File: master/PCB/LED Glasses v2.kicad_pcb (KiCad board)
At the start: 2 copper layers, 152.9 x 54.6 mm, 85 parts, among them J1 Conn_01x01_Male, J2 Conn_01x01_Male, J3 Conn_01x01_Male, J4 Conn_01x01_Male, J5 Conn_01x01_Male

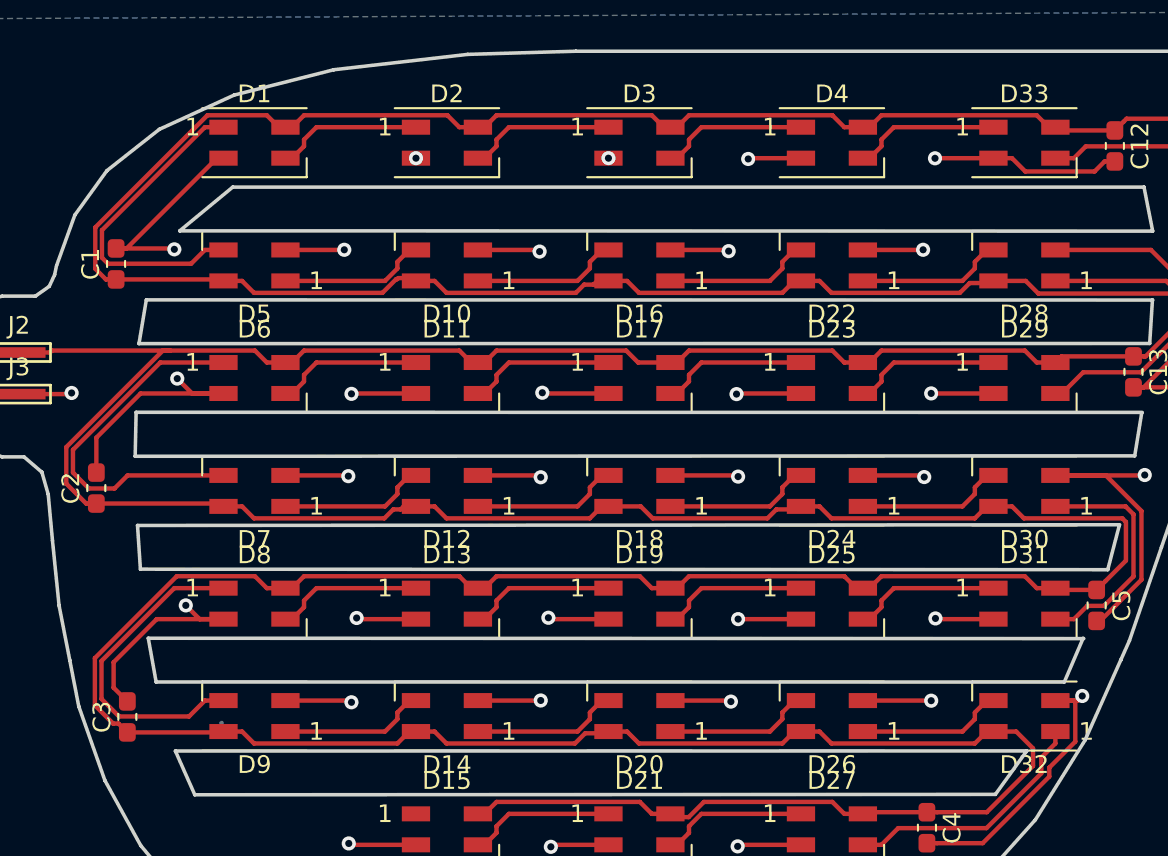
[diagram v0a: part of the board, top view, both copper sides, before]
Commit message: Added silkscreen
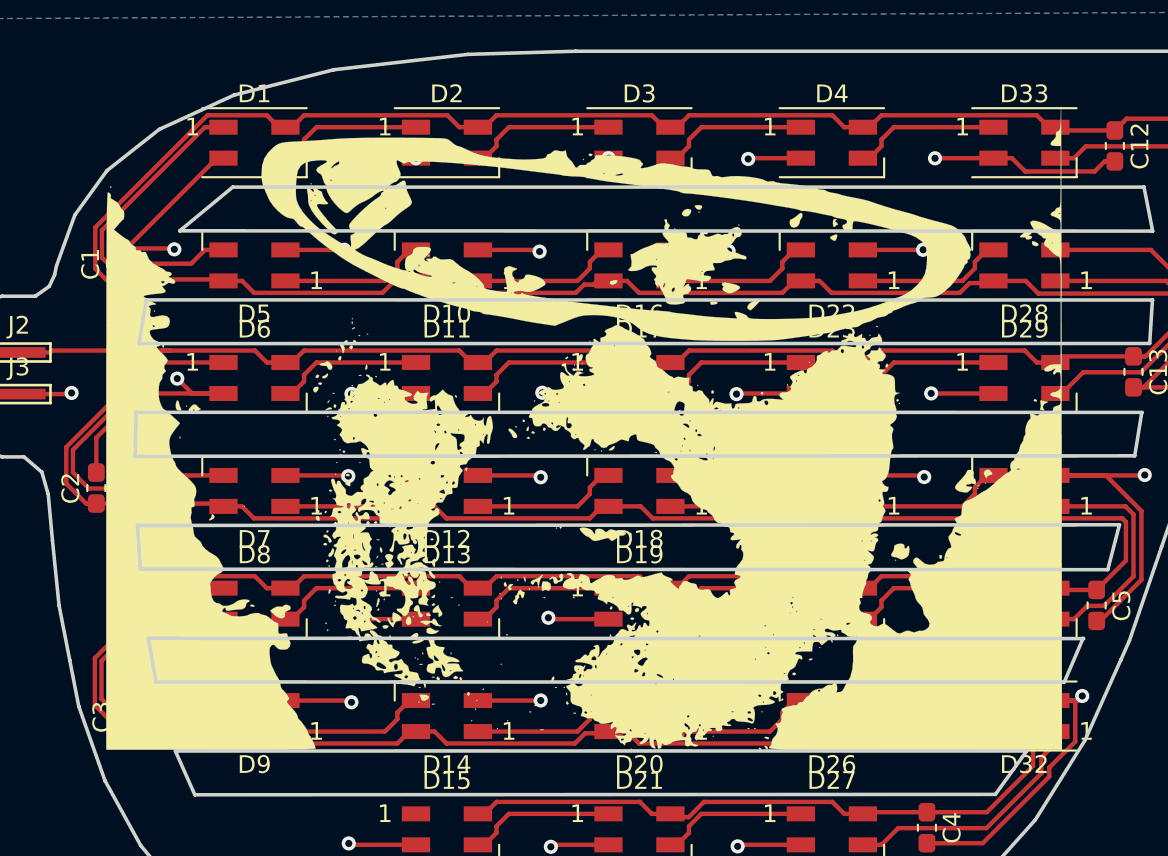
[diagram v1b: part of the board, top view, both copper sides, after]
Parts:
- added G***: LOGO-glasses, Battery:LOGO-glasses, F.Cu at (120.6, 104.3)

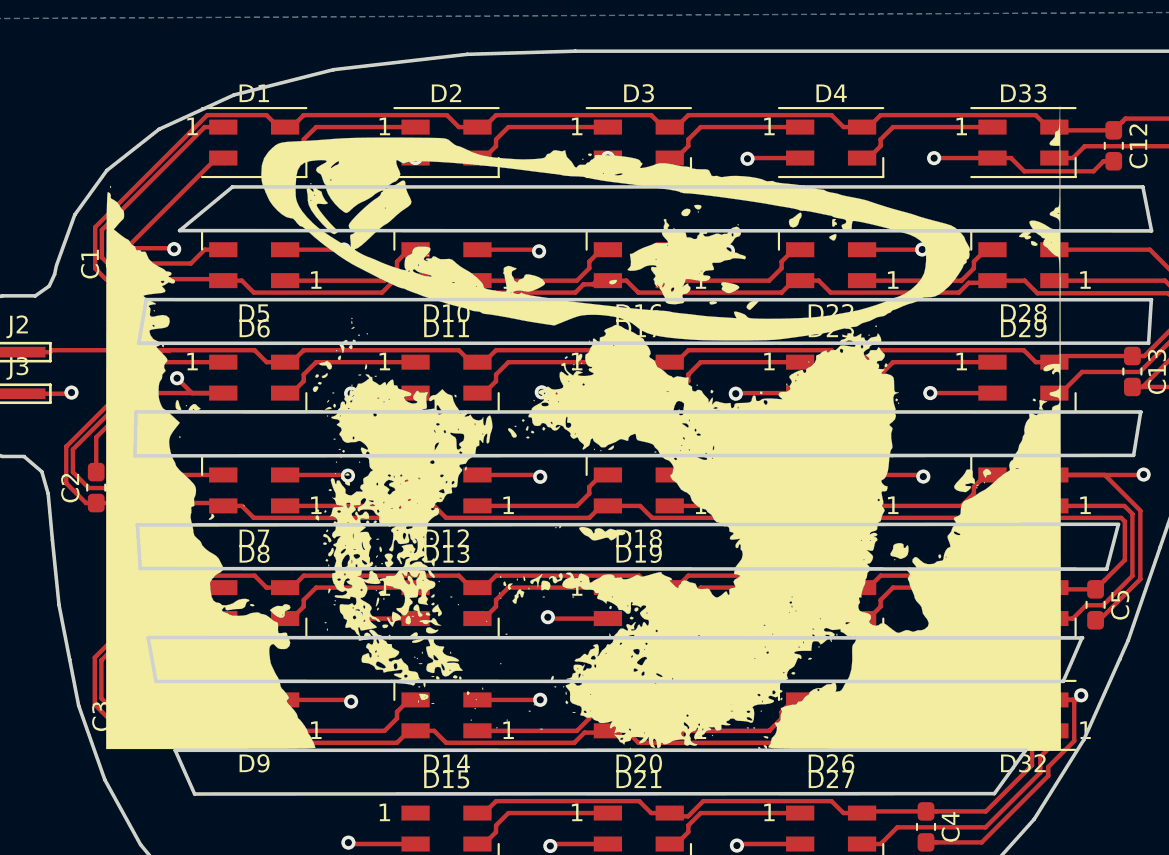
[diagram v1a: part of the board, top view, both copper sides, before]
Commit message: added silkscreen
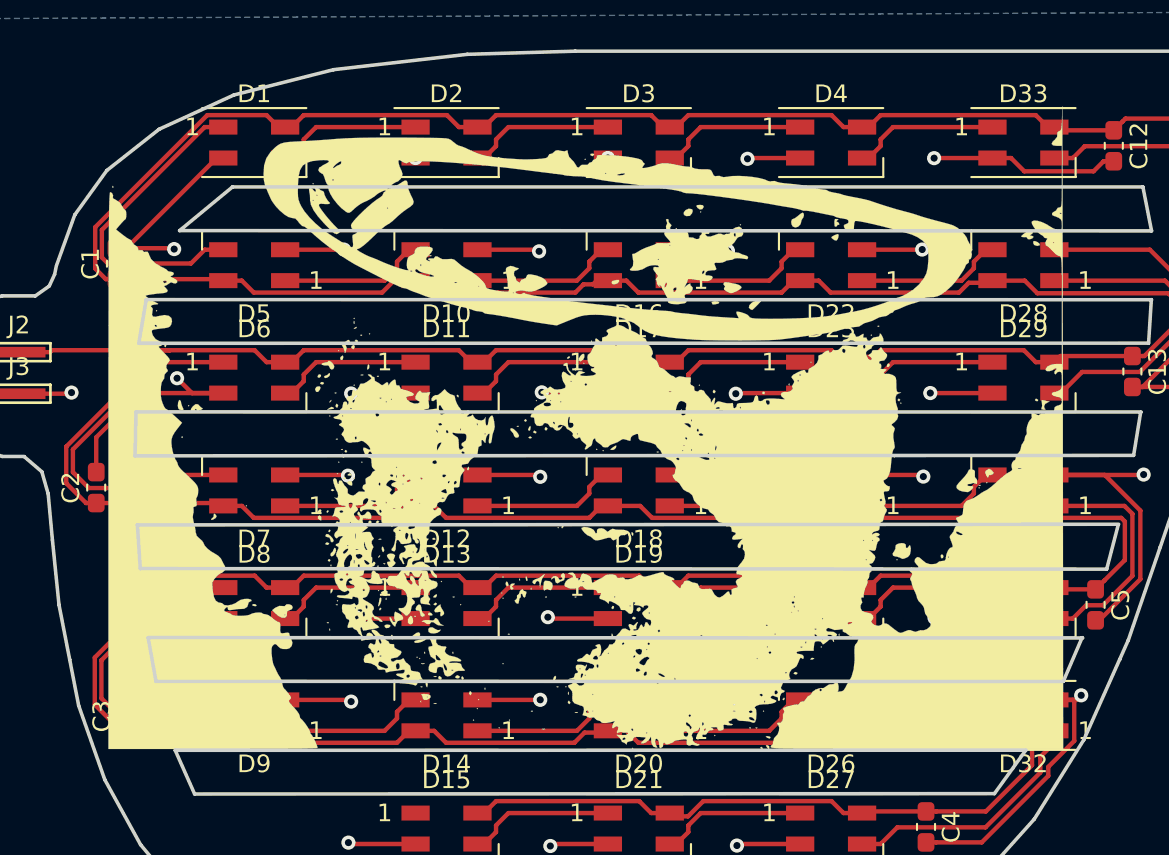
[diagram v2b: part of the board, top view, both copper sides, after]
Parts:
- moved G*** 0.13 mm to (120.8, 104.3)

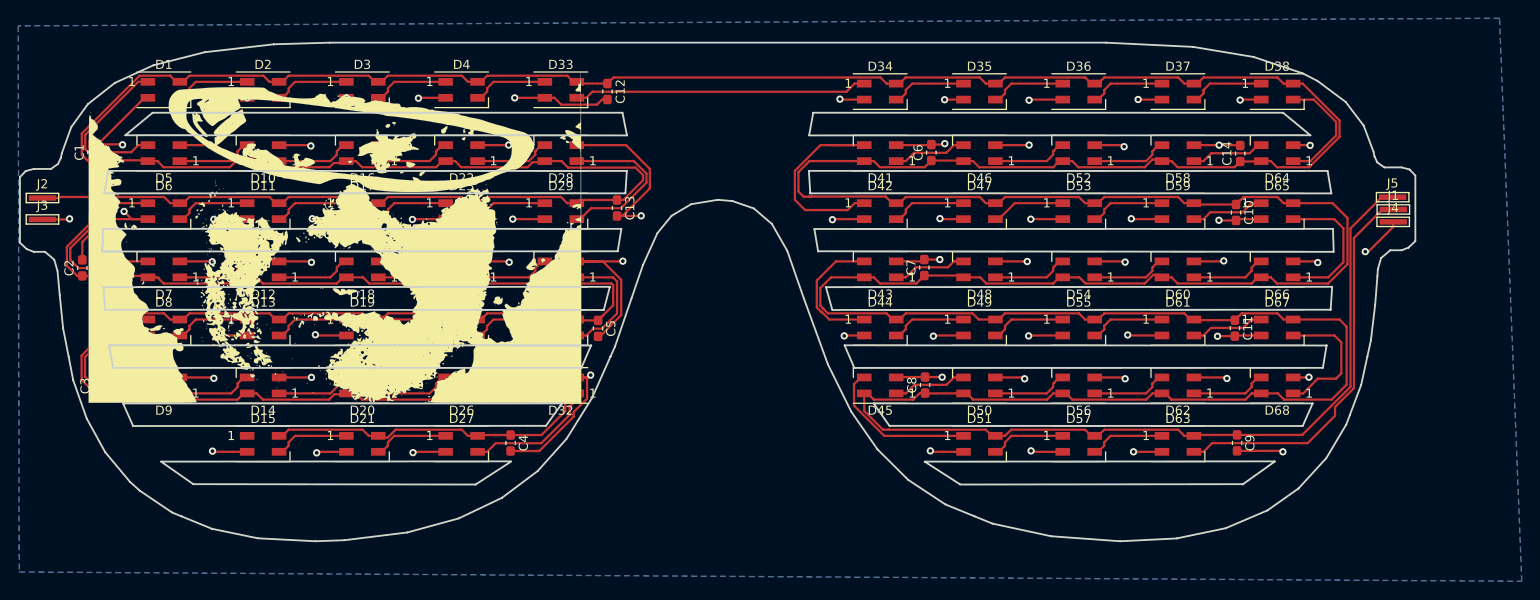
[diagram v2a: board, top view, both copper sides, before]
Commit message: moved logo to back silkscreen
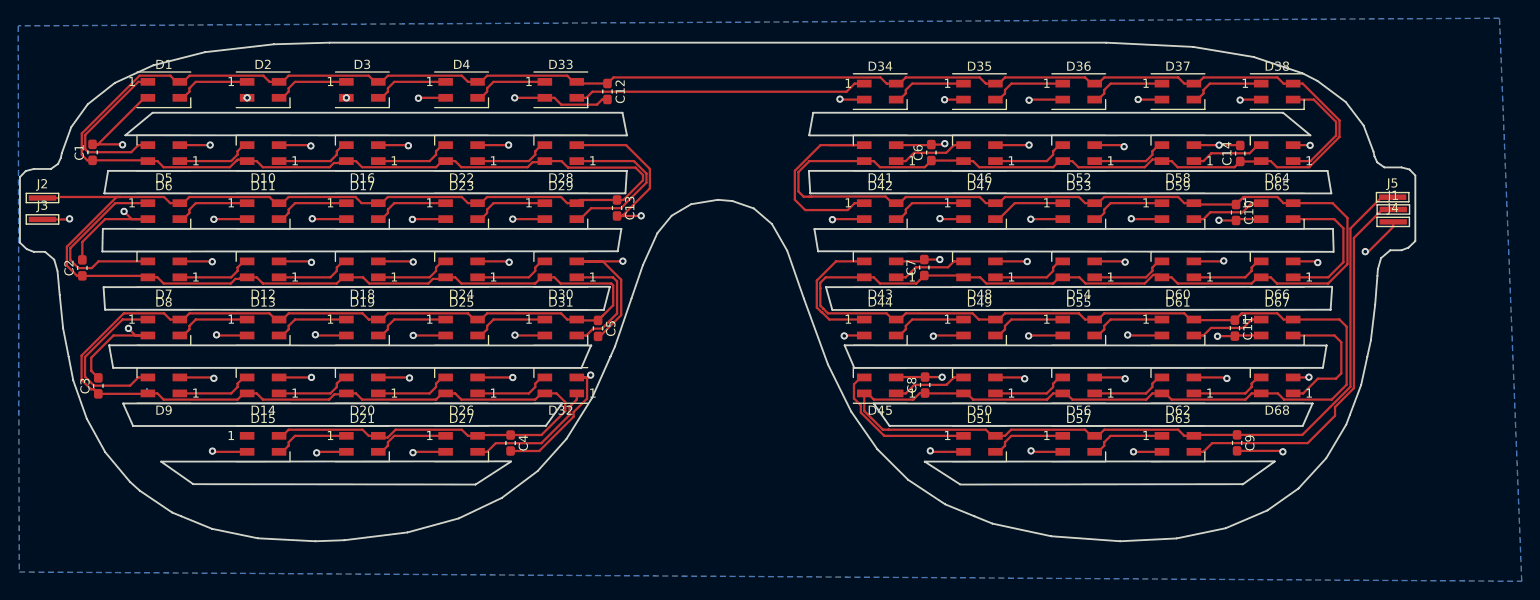
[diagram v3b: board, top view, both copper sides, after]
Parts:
- removed the G*** at (120.8, 104.3)
- added G***: LOGO, Lachlan_Modules:back_silkscreen, F.Cu at (121.2, 104.0)
